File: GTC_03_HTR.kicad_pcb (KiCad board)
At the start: 2 copper layers, 67.8 x 86.9 mm, 21 parts, among them J1 TB_PhxContact_MKDS-1.5-3-5.08, J2 TB_PhxContact_MKDS-1.5-3-5.08, J3 TB_PhxContact_MKDS-1.5-3-5.08, J4 TB_PhxContact_MKDS-1.5-3-5.08, J5 TB_PhxContact_MKDS-1.5-3-5.08, Q1 MOSFET_STP40NF10L, Q2 MOSFET_STP40NF10L

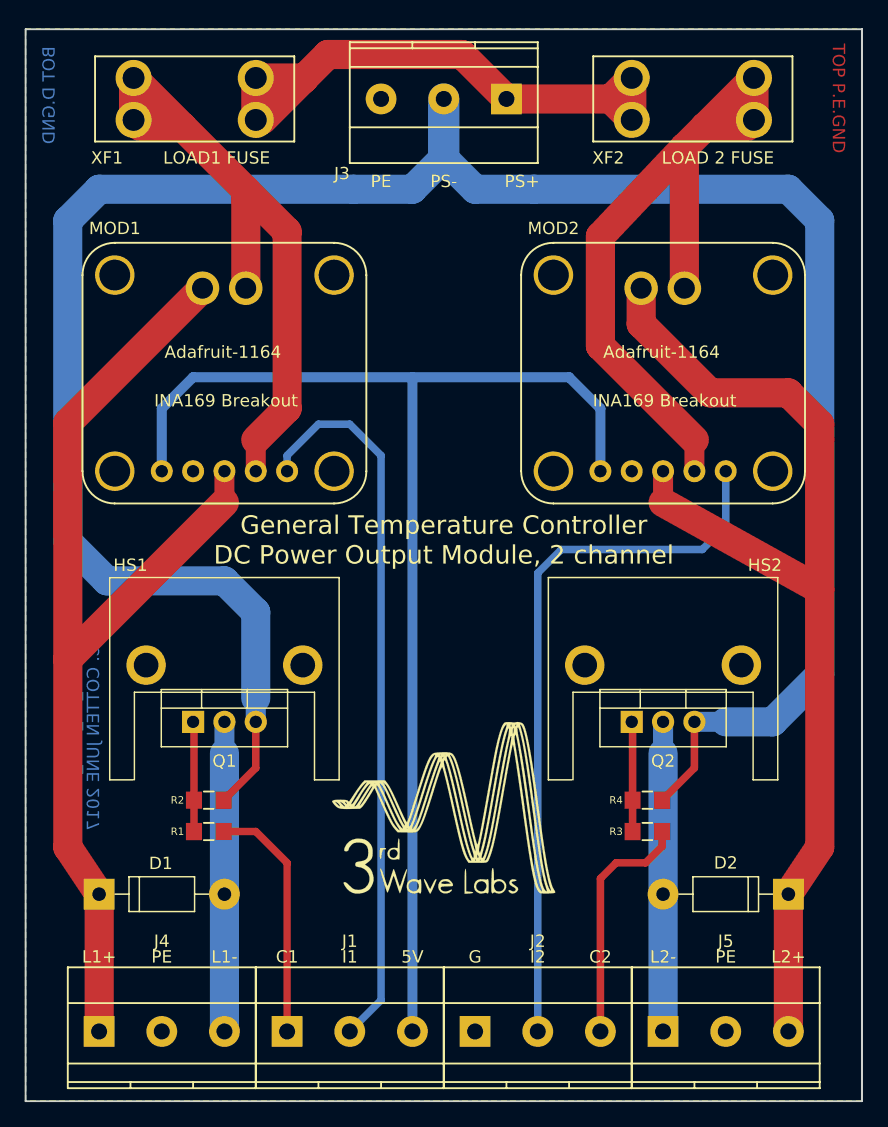
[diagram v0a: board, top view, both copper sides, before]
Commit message: changed Cu text per fab house recommendation
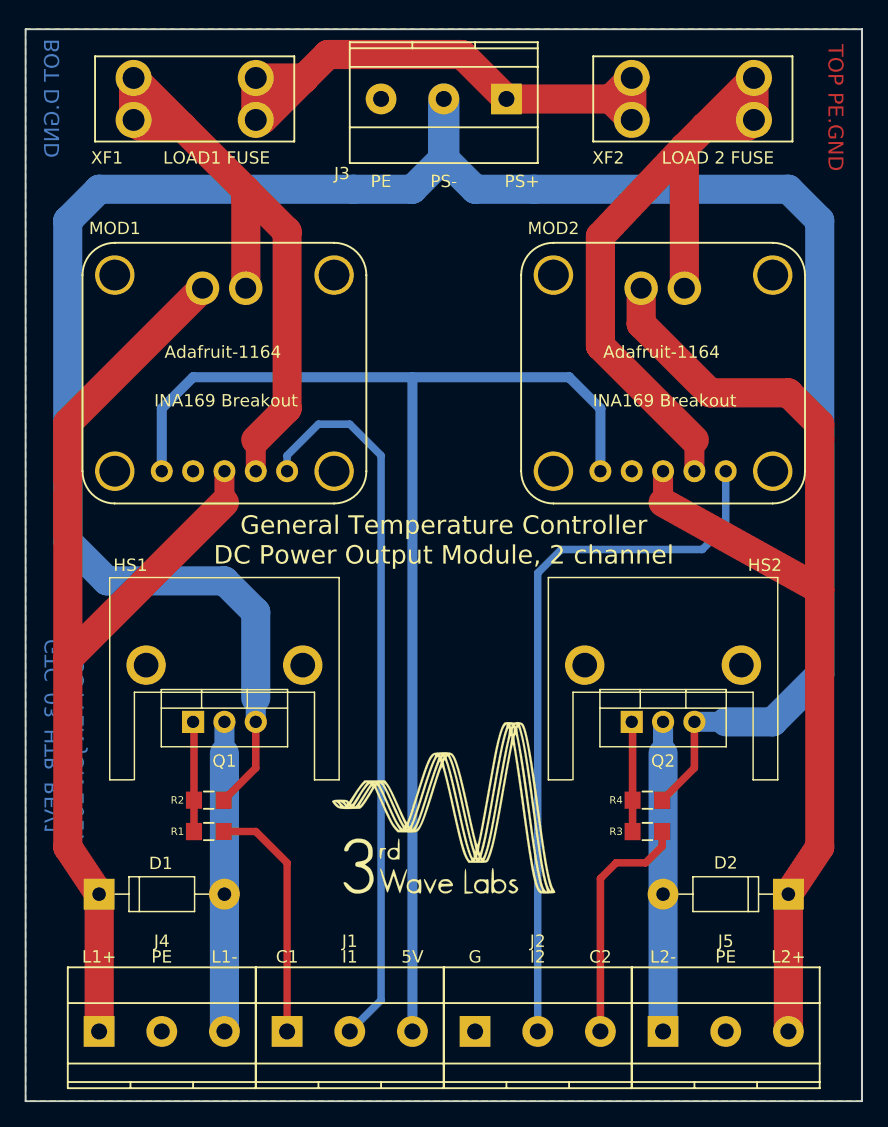
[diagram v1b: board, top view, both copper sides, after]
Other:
- board text added: "GTC_03_HTR_REV1 C. COTTEN JUN 2017"
- board text added: "TOP PE.GND"
- board text removed: "GTC_03_HTR_REV1 C. COTTEN JUNE 2017"
- board text removed: "TOP P.E.GND"
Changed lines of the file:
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@@
   (title_block
     (title "GTC Module 03: DC Power Output Module")
-    (date 2017-06-26)
+    (date 2017-06-30)
     (rev 1)
     (company "3rd Wave Labs")
@@
     (38 B.Mask user)
     (39 F.Mask user)
-    (40 Dwgs.User user)
-    (41 Cmts.User user)
+    (40 Dwgs.User user hide)
+    (41 Cmts.User user hide)
     (42 Eco1.User user)
-    (43 Eco2.User user)
+    (43 Eco2.User user hide)
     (44 Edge.Cuts user)
     (45 Margin user hide)
     (46 B.CrtYd user)
-    (47 F.CrtYd user)
+    (47 F.CrtYd user hide)
     (48 B.Fab user)
     (49 F.Fab user)
   )
   (setup
-    (last_trace_width 0.254)
+    (last_trace_width 1.6256)
     (user_trace_width 0.2032)
     (user_trace_width 0.3048)
@@
       (psnegative false)
       (psa4output false)
-      (plotreference true)
-      (plotvalue true)
+      (plotreference false)
+      (plotvalue false)
       (plotinvisibletext false)
       (padsonsilk false)
@@
       (drillshape 0)
       (scaleselection 1)
-      (outputdirectory GERBER/))
+      (outputdirectory GERBER_06302017/))
   )
   (net 0 "")
@@
     (effects (font (size 1.5 1.5) (thickness 0.3)))
   )
-  (gr_text "GTC_03_HTR_REV1\nC. COTTEN JUNE 2017" (at 115.57 108.47 90) (layer B.Cu)
-    (effects (font (size 1 1) (thickness 0.15)) (justify mirror))
+  (gr_text "GTC_03_HTR_REV1\nC. COTTEN JUN 2017" (at 114.046 108.47 90) (layer B.Cu)
+    (effects (font (size 1.2192 1.2192) (thickness 0.3048)) (justify mirror))
   )
   (gr_text PE (at 121.92 126.25) (layer F.SilkS)
@@
     (effects (font (size 1 1) (thickness 0.15)))
   )
-  (gr_text "TOP P.E.GND" (at 176.784 56.654 270) (layer F.Cu)
-    (effects (font (size 1 1) (thickness 0.15)))
+  (gr_text "TOP PE.GND" (at 176.53 57.416 270) (layer F.Cu)
+    (effects (font (size 1.2192 1.2192) (thickness 0.3048)))
   )
   (gr_text PS- (at 144.78 63.385) (layer F.SilkS)
@@
     (effects (font (size 1 1) (thickness 0.15)))
   )
-  (gr_text "BOT D.GND" (at 112.776 56.4 90) (layer B.Cu)
-    (effects (font (size 1 1) (thickness 0.15)) (justify mirror))
+  (gr_text "BOT D.GND" (at 113.03 56.654 90) (layer B.Cu)
+    (effects (font (size 1.2192 1.2192) (thickness 0.3048)) (justify mirror))
   )
   (gr_line (start 110.88 137.95) (end 110.88 51.05) (angle 90) (layer Edge.Cuts) (width 0.15))
@@
   (segment (start 162.56 132.3) (end 162.56 121.17) (width 2.3622) (layer B.Cu) (net 4))
   (segment (start 132.08 86.88) (end 132.08 85.61) (width 0.6096) (layer B.Cu) (net 9))
+  (segment (start 132.08 85.61) (end 134.62 83.07) (width 0.6096) (layer B.Cu) (net 9))
+  (segment (start 134.62 83.07) (end 137.16 83.07) (width 0.6096) (layer B.Cu) (net 9))
+  (segment (start 137.16 83.07) (end 139.7 85.61) (width 0.6096) (layer B.Cu) (net 9))
+  (segment (start 139.7 85.61) (end 139.7 129.76) (width 0.6096) (layer B.Cu) (net 9))
   (segment (start 139.7 129.76) (end 137.16 132.3) (width 0.6096) (layer B.Cu) (net 9))
-  (segment (start 139.7 85.61) (end 139.7 129.76) (width 0.6096) (layer B.Cu) (net 9))
-  (segment (start 137.16 83.07) (end 139.7 85.61) (width 0.6096) (layer B.Cu) (net 9))
-  (segment (start 134.62 83.07) (end 137.16 83.07) (width 0.6096) (layer B.Cu) (net 9))
-  (segment (start 132.08 85.61) (end 134.62 83.07) (width 0.6096) (layer B.Cu) (net 9))
   (segment (start 167.64 86.88) (end 167.64 91.325) (width 0.6096) (layer B.Cu) (net 10))
   (segment (start 167.64 91.325) (end 165.735 93.23) (width 0.6096) (layer B.Cu) (net 10))
@@
   (segment (start 160.02 58.4) (end 160.0164 58.4) (width 1.6256) (layer F.Cu) (net 13))
   (segment (start 160.0164 58.4) (end 158.3164 56.7) (width 2.3622) (layer F.Cu) (net 13))
-  (segment (start 165.1 107.2) (end 167.64 107.2) (width 1.6256) (layer B.Cu) (net 14))
-  (segment (start 171.45 107.2) (end 175.26 103.39) (width 2.3622) (layer B.Cu) (net 14))
-  (segment (start 175.26 103.39) (end 175.26 66.56) (width 2.3622) (layer B.Cu) (net 14))
-  (segment (start 175.26 66.56) (end 172.72 64.02) (width 2.3622) (layer B.Cu) (net 14))
-  (segment (start 172.72 64.02) (end 152.1 64.02) (width 2.3622) (layer B.Cu) (net 14))
-  (segment (start 147.32 64.02) (end 144.78 61.48) (width 2.3622) (layer B.Cu) (net 14))
-  (segment (start 152.1 64.02) (end 147.32 64.02) (width 2.3622) (layer B.Cu) (net 14))
-  (segment (start 167.64 107.2) (end 171.45 107.2) (width 2.3622) (layer B.Cu) (net 14))
+  (segment (start 129.54 105.295) (end 129.54 107.2) (width 1.6256) (layer B.Cu) (net 14))
   (segment (start 129.54 98.31) (end 129.54 105.295) (width 2.3622) (layer B.Cu) (net 14))
-  (segment (start 129.54 105.295) (end 129.54 107.2) (width 1.6256) (layer B.Cu) (net 14))
-  (segment (start 144.78 61.48) (end 142.24 64.02) (width 2.3622) (layer B.Cu) (net 14))
+  (segment (start 127 95.77) (end 129.54 98.31) (width 2.3622) (layer B.Cu) (net 14))
+  (segment (start 117.475 95.77) (end 127 95.77) (width 2.3622) (layer B.Cu) (net 14))
+  (segment (start 142.24 64.02) (end 144.78 61.48) (width 2.3622) (layer B.Cu) (net 14))
   (segment (start 142.24 64.02) (end 137.46 64.02) (width 2.3622) (layer B.Cu) (net 14))
   (segment (start 114.3 88.15) (end 114.3 92.595) (width 2.3622) (layer B.Cu) (net 14))
   (segment (start 114.3 92.595) (end 117.475 95.77) (width 2.3622) (layer B.Cu) (net 14))
-  (segment (start 117.475 95.77) (end 127 95.77) (width 2.3622) (layer B.Cu) (net 14))
-  (segment (start 127 95.77) (end 129.54 98.31) (width 2.3622) (layer B.Cu) (net 14))
   (segment (start 116.84 64.02) (end 137.46 64.02) (width 2.3622) (layer B.Cu) (net 14))
   (segment (start 114.3 66.56) (end 116.84 64.02) (width 2.3622) (layer B.Cu) (net 14))
   (segment (start 114.3 88.15) (end 114.3 66.56) (width 2.3622) (layer B.Cu) (net 14))
+  (segment (start 165.1 107.2) (end 167.64 107.2) (width 1.6256) (layer B.Cu) (net 14))
+  (segment (start 167.64 107.2) (end 171.45 107.2) (width 2.3622) (layer B.Cu) (net 14))
+  (segment (start 152.1 64.02) (end 147.32 64.02) (width 2.3622) (layer B.Cu) (net 14))
+  (segment (start 147.32 64.02) (end 144.78 61.48) (width 2.3622) (layer B.Cu) (net 14))
+  (segment (start 172.72 64.02) (end 152.1 64.02) (width 2.3622) (layer B.Cu) (net 14))
+  (segment (start 175.26 66.56) (end 172.72 64.02) (width 2.3622) (layer B.Cu) (net 14))
+  (segment (start 175.26 103.39) (end 175.26 66.56) (width 2.3622) (layer B.Cu) (net 14))
+  (segment (start 171.45 107.2) (end 175.26 103.39) (width 2.3622) (layer B.Cu) (net 14))
   (segment (start 144.78 56.7) (end 144.78 61.48) (width 2.54) (layer B.Cu) (net 14))
   (segment (start 165.1 107.2) (end 165.1 110.94) (width 0.6096) (layer F.Cu) (net 14))

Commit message: GTC_03_HTR_REV1, 3oz. Cu, 6/30/2017
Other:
- board text added: "GTC_03_HTR_REV1 3oz / 10A"
- board text removed: "GTC_03_HTR_REV1 C. COTTEN JUN 2017"
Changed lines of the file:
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@@
   )
   (layers
-    (0 F.Cu signal)
+    (0 F.Cu signal hide)
     (31 B.Cu signal)
     (32 B.Adhes user hide)
@@
   )
   (setup
-    (last_trace_width 1.6256)
+    (last_trace_width 0.254)
     (user_trace_width 0.2032)
     (user_trace_width 0.3048)
@@
     (effects (font (size 1.5 1.5) (thickness 0.3)))
   )
-  (gr_text "GTC_03_HTR_REV1\nC. COTTEN JUN 2017" (at 114.046 108.47 90) (layer B.Cu)
+  (gr_text "GTC_03_HTR_REV1\n3oz / 10A" (at 114.046 108.47 90) (layer B.Cu)
     (effects (font (size 1.2192 1.2192) (thickness 0.3048)) (justify mirror))
   )

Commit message: GTC_03_HTR_REV1, 1oz Cu, 6/30/2017
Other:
- board text added: "GTC_03_HTR_REV1 1oz / 4.5A"
- board text removed: "GTC_03_HTR_REV1 3oz / 10A"
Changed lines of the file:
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@@
     (effects (font (size 1.5 1.5) (thickness 0.3)))
   )
-  (gr_text "GTC_03_HTR_REV1\n3oz / 10A" (at 114.046 108.47 90) (layer B.Cu)
+  (gr_text "GTC_03_HTR_REV1\n1oz / 4.5A" (at 114.046 108.47 90) (layer B.Cu)
     (effects (font (size 1.2192 1.2192) (thickness 0.3048)) (justify mirror))
   )
